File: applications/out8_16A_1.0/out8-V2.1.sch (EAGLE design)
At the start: 29 parts, among them IC1 ULN2803, IC2 ULN2803, K1 HFE20-1-024-1HD504, K2 HFE20-1-024-1HD504, K3 HFE20-1-024-1HD504, K4 HFE20-1-024-1HD504, K5 HFE20-1-024-1HD504, K6 HFE20-1-024-1HD504, K7 HFE20-1-024-1HD504, K8 HFE20-1-024-1HD504

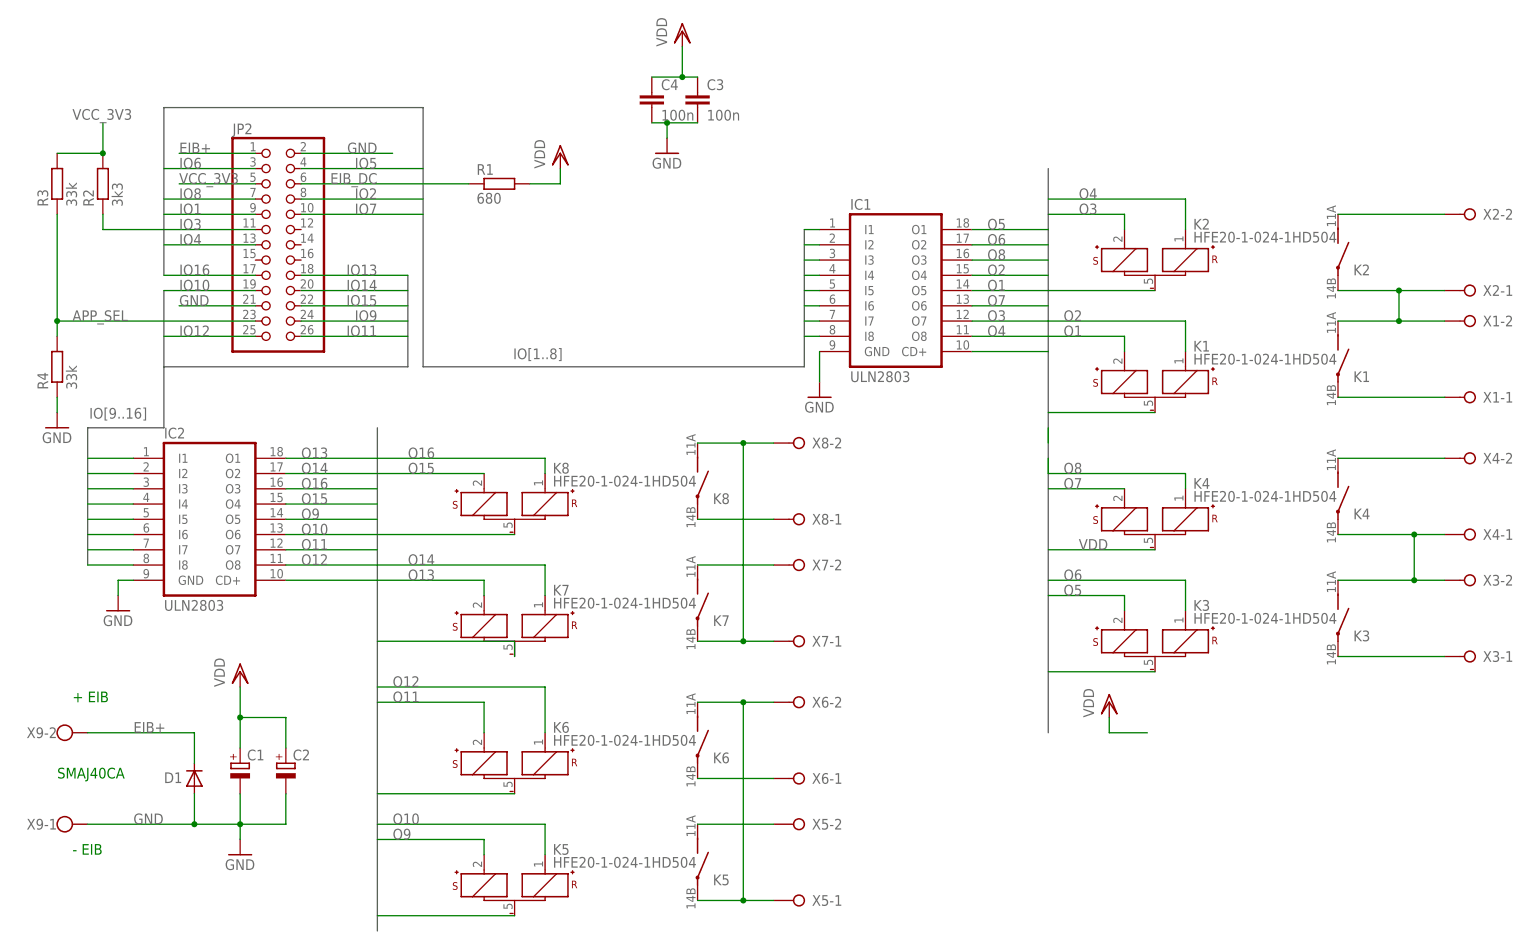
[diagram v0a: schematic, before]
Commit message: Hint for usage of R2 added.
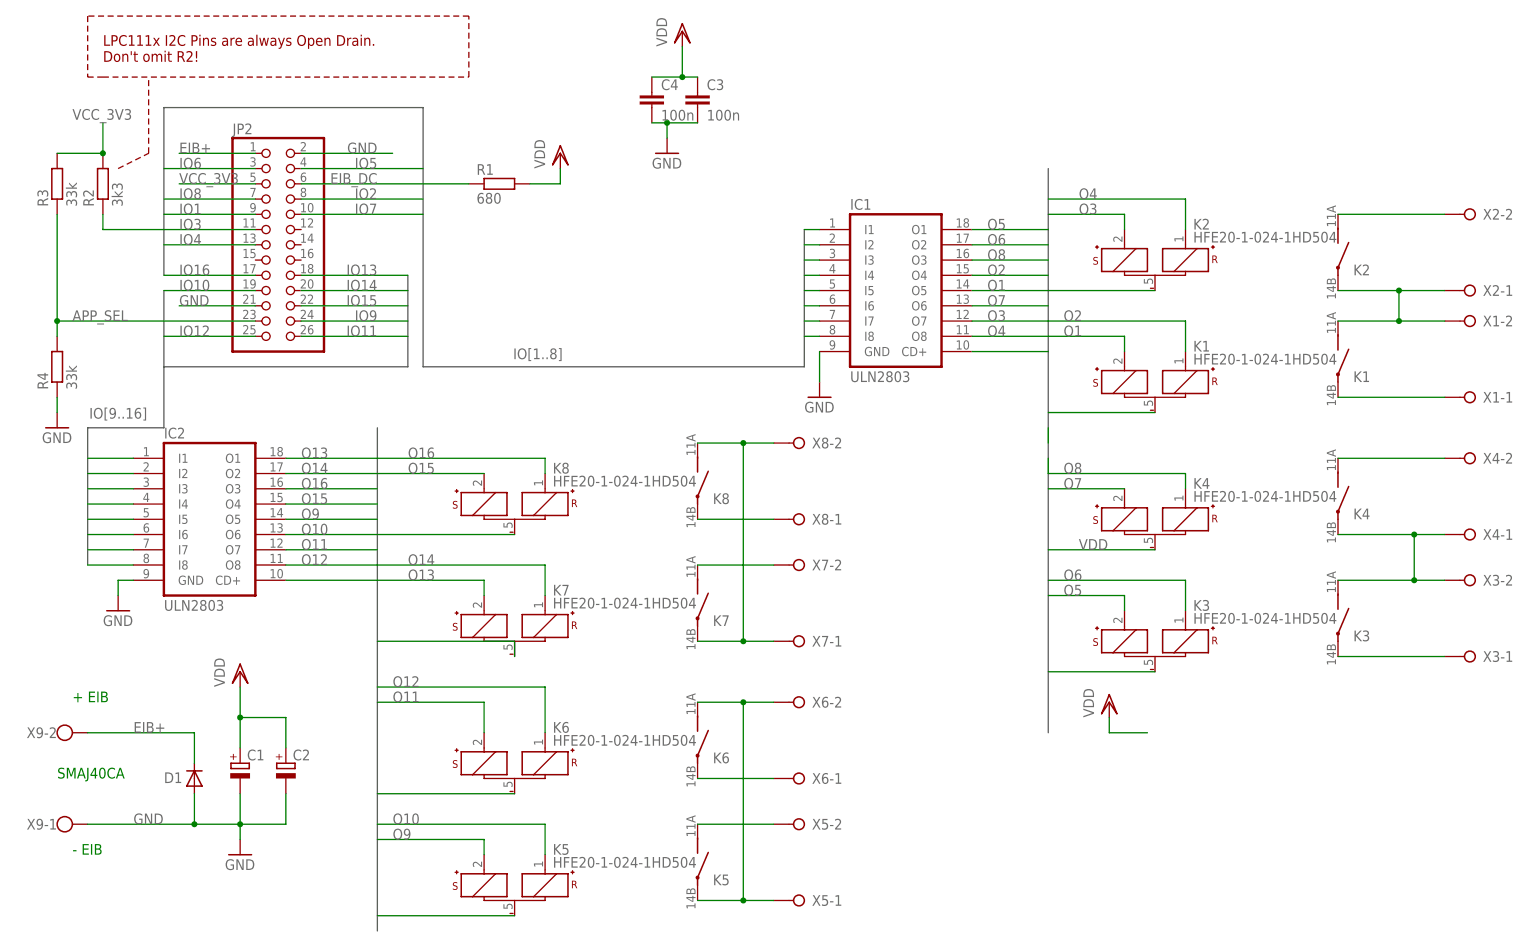
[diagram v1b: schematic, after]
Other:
- note added: "LPC111x I2C Pins are always Open Drain. Don't omit R2!"
